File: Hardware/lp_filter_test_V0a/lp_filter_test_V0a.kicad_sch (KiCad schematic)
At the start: 8 parts, among them U1 BD450M5FP-CE2, U2 MAX7480ESA+

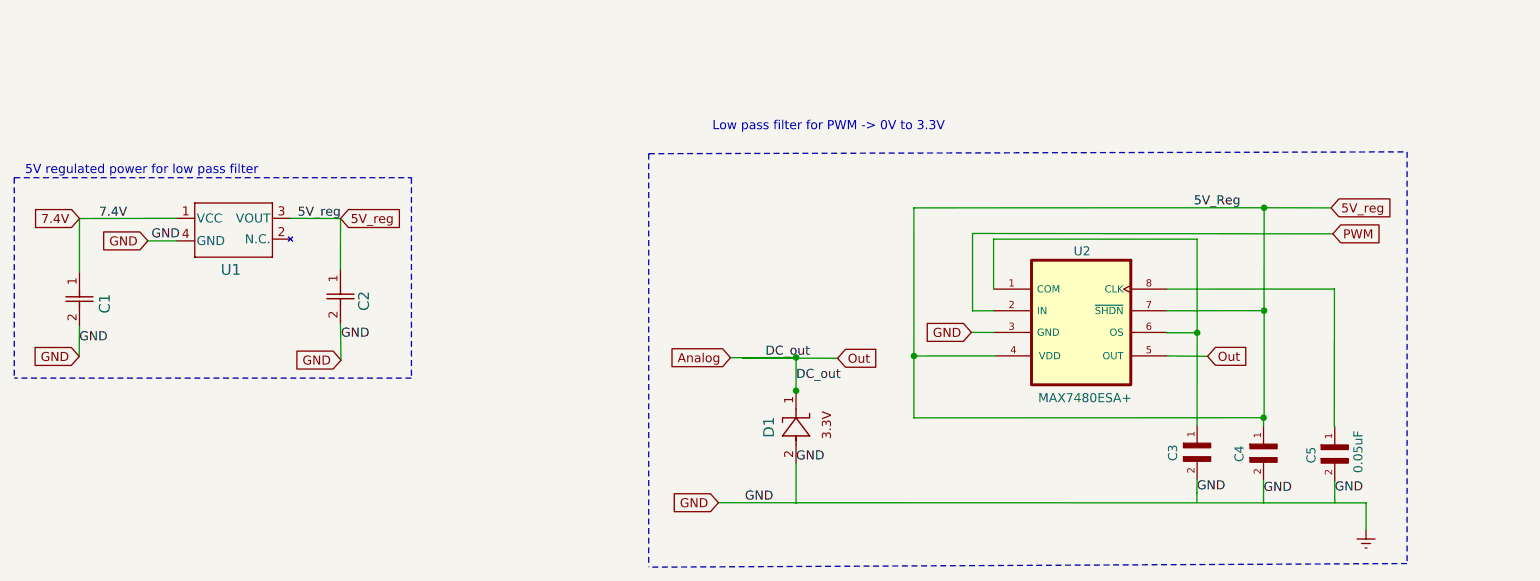
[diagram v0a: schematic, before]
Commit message: Updating lp filter test project
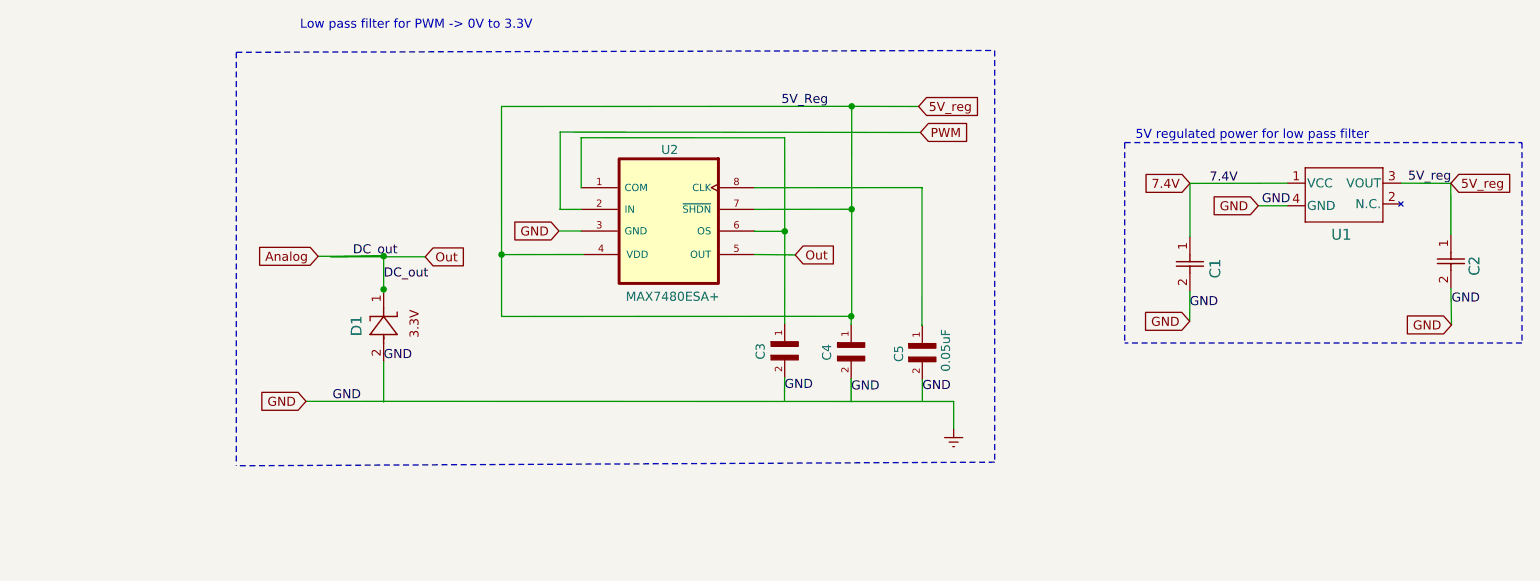
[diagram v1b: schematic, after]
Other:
- moved on the sheet: C1, C2, C3, C4, C5, D1, U1, U2
